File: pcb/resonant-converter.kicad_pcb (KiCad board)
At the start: 4 copper layers, 100 x 100 mm, 144 parts, among them J1 Banana_Jack_Keystone_575-8, J2 Banana_Jack_Keystone_575-8, J3 Banana_Jack_Keystone_575-8, J4 Banana_Jack_Keystone_575-8, J5 Molex_KK_1x4_0470531000, J6 JST_SH_1x4_BM04B-SRSS-TB-LF-SN, Q1 HSU30N20, Q2 HSU30N20, Q3 MDU04N010VRH, Q4 MDU04N010VRH, T1 B66206W1110T001, U1 UCC256610DDBR, U2 TEA2096T/1J, U3 78L15MG, U4 PC817X2CSP9F, U5 TL431AIDBVR, U6 INA219BIDCNR

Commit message: WIP: Layout PCB secondary side
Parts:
- moved R34 27.4 mm to (186.2, 102.2), turned to 90 degrees
- moved C49 26.9 mm to (184.8, 103.8), turned to 180 degrees
- moved R35 26.5 mm to (187.3, 102.2), turned to 90 degrees
- moved C48 25.2 mm to (186.7, 103.8), turned to 0 degrees
- moved U6 23.5 mm to (185.7, 106.2), turned to -90 degrees
- moved TP11 22.5 mm to (186.3, 119.8)
- moved TP7 22.5 mm to (190.3, 114.5)
- moved R36 21.8 mm to (184.8, 109.3), turned to 180 degrees
- moved R37 19.6 mm to (186.7, 109.3), turned to 0 degrees
- moved TP22 18.9 mm to (184.2, 116.3), turned to -90 degrees
- moved J6 18.6 mm to (185.7, 112.1), turned to 0 degrees
- moved D10 17.6 mm to (181.1, 111.3), turned to -90 degrees
- moved D9 17.5 mm to (195.3, 102.5), turned to 180 degrees
- moved kibuzzard-69E92ECD 17.4 mm to (179.9, 111.3), turned to 90 degrees
- moved R38 17.4 mm to (181.1, 113.6), turned to -90 degrees
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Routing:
- net Net-(Q4-G): track 0.00 -> 7.36 mm
- net Net-(Q3-G): track 0.00 -> 7.27 mm
- net Net-(D6-C): track 0.00 -> 7.01 mm, vias 0 -> 2
- net Net-(D5-C): track 0.00 -> 6.75 mm, vias 0 -> 2
- net /+12V_R: track 0.00 -> 3.67 mm, vias 0 -> 1
- net +12V: track 3.19 -> 5.76 mm
- net GND_ISO: track 8.42 -> 8.11 mm, vias 9 -> 38
- added copper zone on F.Cu, net +12V
- added copper zone on B.Cu, net /+12V_R
- added copper zone on F.Cu, net Net-(D5-C)
- added copper zone on F.Cu, net Net-(D6-C)

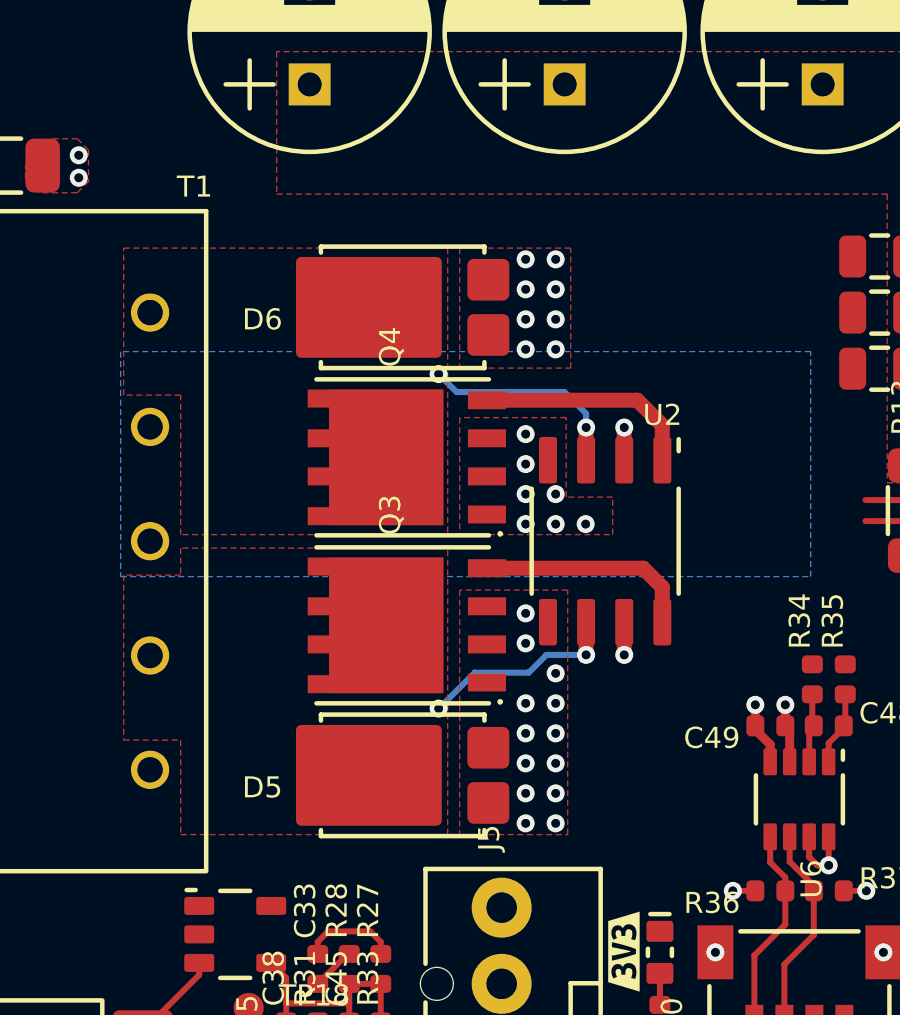
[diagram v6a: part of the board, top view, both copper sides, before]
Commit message: PCB: Layout the rectifier
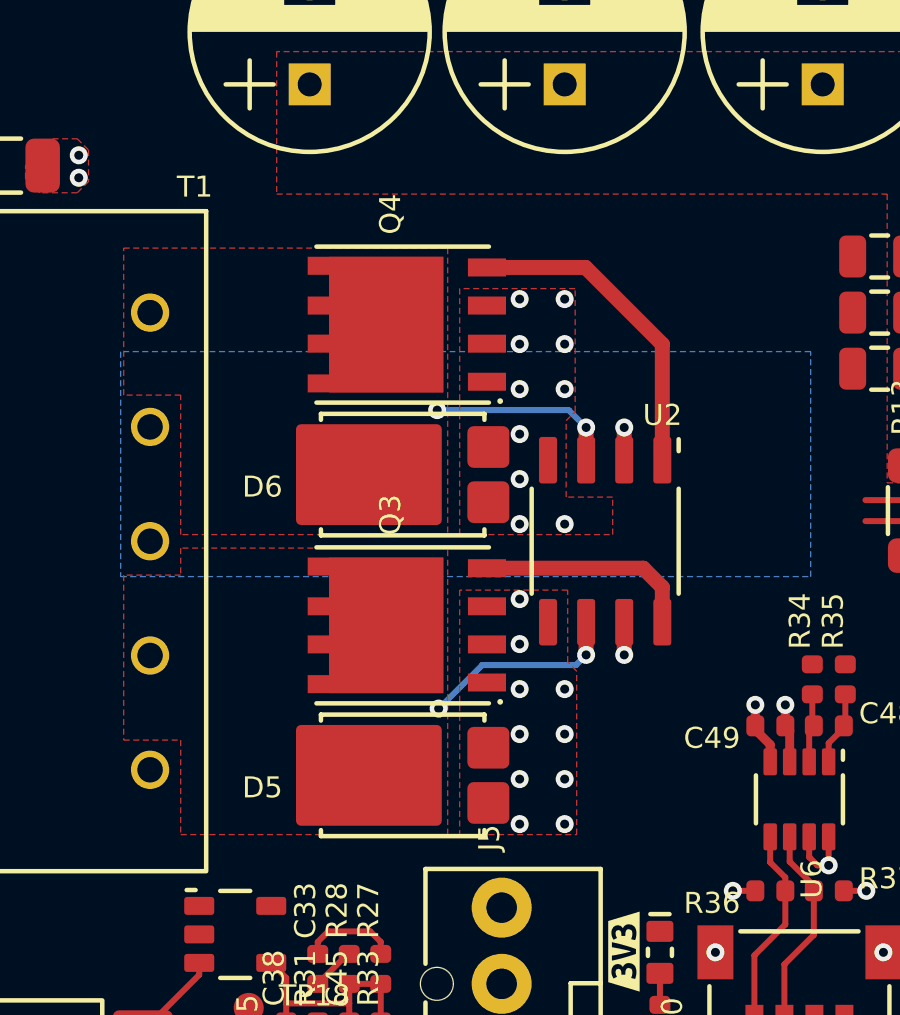
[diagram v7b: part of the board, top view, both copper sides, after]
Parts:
- moved D6 5.57 mm to (172.5, 95.4)
- moved Q4 4.43 mm to (172.5, 90.4)
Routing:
- net Net-(Q4-G): track 7.36 -> 10.8 mm
- net Net-(D6-C): track 7.01 -> 6.30 mm
- net GND_ISO: vias 38 -> 30
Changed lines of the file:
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@@
 	(footprint "DW-footprints:PowerDI-5"
 		(layer "F.Cu")
-		(at 172.5 89.825003 180)
+		(at 172.5 95.4 180)
 		(property "Reference" "D6"
 			(at 4 0 0)
@@
 	(footprint "DW-footprints:PDFN-56-8"
 		(layer "F.Cu")
-		(at 172.5 94.825003 90)
+		(at 172.5 90.4 90)
 		(descr "5x6mm Power DFN, 1.27mm pitch")
 		(tags "PDFN56, 	PDFN-56-8")
@@
 	)
 	(via
-		(at 178.6 97.05)
-		(size 0.6)
-		(drill 0.3)
-		(layers "F.Cu" "B.Cu")
-		(net 17)
-	)
-	(via
 		(at 179.885 93.83)
 		(size 0.6)
@@
 	)
 	(via
-		(at 188.525 111.325001)
-		(size 0.6)
-		(drill 0.3)
-		(layers "F.Cu" "B.Cu")
-		(net 17)
-	)
-	(via
-		(at 177.6 91.224998)
+		(at 176.4 101.05)
 		(size 0.6)
 		(drill 0.3)
@@
 	)
 	(via
-		(at 177.6 97.05)
+		(at 177.9 97.05)
 		(size 0.6)
 		(drill 0.3)
@@
 	)
 	(via
-		(at 177.6 105.025)
+		(at 188.525 111.325001)
 		(size 0.6)
 		(drill 0.3)
@@
 	)
 	(via
-		(at 177.6 102.025005)
+		(at 176.4 94.05)
 		(size 0.6)
 		(drill 0.3)
@@
 	)
 	(via
-		(at 177.6 88.225003)
+		(at 176.4 91.05)
 		(size 0.6)
 		(drill 0.3)
@@
 	)
 	(via
-		(at 176.6 105.025)
+		(at 176.4 105.55)
 		(size 0.6)
 		(drill 0.3)
@@
 	)
 	(via
-		(at 176.6 94.050005)
+		(at 177.9 91.05)
 		(size 0.6)
 		(drill 0.3)
@@
 	)
 	(via
-		(at 176.6 103.025003)
+		(at 176.4 89.55)
 		(size 0.6)
 		(drill 0.3)
@@
 	)
 	(via
-		(at 176.6 97.05)
+		(at 177.9 102.55)
 		(size 0.6)
 		(drill 0.3)
@@
 	)
 	(via
-		(at 172.46837 116.876903)
+		(at 176.4 102.55)
 		(size 0.6)
 		(drill 0.3)
@@
 	)
 	(via
-		(at 176.6 90.224998)
+		(at 176.4 99.55)
 		(size 0.6)
 		(drill 0.3)
@@
 	)
 	(via
-		(at 182.925 111.325001)
+		(at 177.9 105.55)
 		(size 0.6)
 		(drill 0.3)
@@
 	)
 	(via
-		(at 176.6 107.024998)
+		(at 176.4 97.05)
 		(size 0.6)
 		(drill 0.3)
@@
 	)
 	(via
-		(at 176.6 91.224998)
+		(at 172.46837 116.876903)
 		(size 0.6)
 		(drill 0.3)
@@
 	)
 	(via
-		(at 177.6 90.224998)
+		(at 177.9 89.55)
 		(size 0.6)
 		(drill 0.3)
@@
 	)
 	(via
-		(at 177.6 104.025003)
+		(at 182.925 111.325001)
 		(size 0.6)
 		(drill 0.3)
@@
 	)
 	(via
-		(at 176.6 89.225)
-		(size 0.6)
-		(drill 0.3)
-		(layers "F.Cu" "B.Cu")
-		(net 17)
-	)
-	(via
-		(at 176.6 96.05)
-		(size 0.6)
-		(drill 0.3)
-		(layers "F.Cu" "B.Cu")
-		(net 17)
-	)
-	(via
 		(at 187.225 114.975)
 		(size 0.6)
@@
 	)
 	(via
-		(at 176.6 101.025005)
-		(size 0.6)
-		(drill 0.3)
-		(layers "F.Cu" "B.Cu")
-		(net 17)
-	)
-	(via
 		(at 186.7 108.425)
 		(size 0.6)
@@
 	)
 	(via
-		(at 176.6 106.024998)
-		(size 0.6)
-		(drill 0.3)
-		(layers "F.Cu" "B.Cu")
-		(net 17)
-	)
-	(via
-		(at 177.6 96.05)
-		(size 0.6)
-		(drill 0.3)
-		(layers "F.Cu" "B.Cu")
-		(net 17)
-	)
-	(via
 		(at 161.703436 85.505766)
 		(size 0.6)
@@
 	)
 	(via
-		(at 176.6 100.025007)
-		(size 0.6)
-		(drill 0.3)
-		(layers "F.Cu" "B.Cu")
-		(net 17)
-	)
-	(via
-		(at 176.6 95.050002)
+		(at 177.9 92.55)
 		(size 0.6)
 		(drill 0.3)
@@
 	)
 	(via
-		(at 177.6 103.025003)
+		(at 176.4 107.05)
 		(size 0.6)
 		(drill 0.3)
@@
 	)
 	(via
-		(at 177.6 89.225)
+		(at 176.4 104.05)
 		(size 0.6)
 		(drill 0.3)
@@
 	)
 	(via
-		(at 176.6 88.225003)
+		(at 176.4 95.55)
 		(size 0.6)
 		(drill 0.3)
@@
 	)
 	(via
-		(at 177.6 107.024998)
+		(at 177.9 107.05)
 		(size 0.6)
 		(drill 0.3)
@@
 	)
 	(via
-		(at 176.6 104.025003)
+		(at 177.9 104.05)
 		(size 0.6)
 		(drill 0.3)
@@
 	)
 	(via
-		(at 177.6 106.024998)
+		(at 176.4 92.55)
 		(size 0.6)
 		(drill 0.3)
@@
 	)
 	(segment
-		(start 181.155 93.755)
-		(end 181.155 94.92)
+		(start 178.595001 88.495001)
+		(end 175.31 88.495001)
 		(width 0.5)
 		(layer "F.Cu")
@@
 	)
 	(segment
-		(start 175.31 92.920004)
-		(end 180.320004 92.920004)
+		(start 181.155 94.92)
+		(end 181.155 91.055)
 		(width 0.5)
 		(layer "F.Cu")
@@
 	)
 	(segment
-		(start 180.320004 92.920004)
-		(end 181.155 93.755)
+		(start 181.155 91.055)
+		(end 178.595001 88.495001)
 		(width 0.5)
 		(layer "F.Cu")
@@
 	)
 	(segment
-		(start 174.9 102)
-		(end 176.7 102)
-		(width 0.2)
-		(layer "B.Cu")
-		(net 21)
-	)
-	(segment
-		(start 176.7 102)
-		(end 177.290001 101.409999)
+		(start 175.15 101.75)
+		(end 178.274999 101.75)
 		(width 0.2)
 		(layer "B.Cu")
@@
 	(segment
 		(start 173.7 103.2)
-		(end 174.9 102)
+		(end 175.15 101.75)
 		(width 0.2)
 		(layer "B.Cu")
@@
 	)
 	(segment
-		(start 177.290001 101.409999)
+		(start 178.274999 101.75)
 		(end 178.615 101.409999)
 		(width 0.2)
@@
 	)
 	(via
-		(at 178.615 93.83)
+		(at 173.65 93.25)
 		(size 0.6)
 		(drill 0.3)
@@
 	)
 	(via
-		(at 173.7 92.05)
+		(at 178.615 93.83)
 		(size 0.6)
 		(drill 0.3)
@@
 	)
 	(segment
-		(start 178.615 93.365)
-		(end 178.615 93.83)
+		(start 173.65 93.25)
+		(end 178.035 93.25)
 		(width 0.2)
 		(layer "B.Cu")
@@
 	)
 	(segment
-		(start 173.7 92.05)
-		(end 174.3 92.65)
-		(width 0.2)
-		(layer "B.Cu")
-		(net 48)
-	)
-	(segment
-		(start 177.9 92.65)
-		(end 178.615 93.365)
-		(width 0.2)
-		(layer "B.Cu")
-		(net 48)
-	)
-	(segment
-		(start 174.3 92.65)
-		(end 177.9 92.65)
+		(start 178.035 93.25)
+		(end 178.615 93.83)
 		(width 0.2)
 		(layer "B.Cu")
@@
 	)
 	(zone
-		(net 17)
-		(net_name "GND_ISO")
-		(layer "F.Cu")
-		(hatch edge 0.5)
-		(priority 23)
-		(connect_pads yes
-			(clearance 0.3)
-		)
-		(min_thickness 0.25)
-		(filled_areas_thickness no)
-		(fill yes
-			(thermal_gap 0.5)
-			(thermal_bridge_width 0.5)
-			(smoothing fillet)
-			(radius 0.3)
-		)
-		(polygon
-			(pts
-				(xy 174.4 91.85) (xy 178.1 91.85) (xy 178.1 87.85) (xy 174.4 87.85)
-			)
-		)
-	)
-	(zone
 		(net 4)
 		(net_name "GND")
@@
 		(polygon
 			(pts
-				(xy 174.4 97.4) (xy 179.5 97.4) (xy 179.5 96.15) (xy 177.95 96.15) (xy 177.95 93.5) (xy 174.4 93.5)
+				(xy 174.4 97.4) (xy 179.5 97.4) (xy 179.5 96.15) (xy 177.95 96.15) (xy 177.95 93.6) (xy 178.25 93.3)
+				(xy 178.25 89.2) (xy 174.4 89.2)
 			)
 		)
@@
 		(polygon
 			(pts
-				(xy 174.4 107.4) (xy 178 107.4) (xy 178 99.25) (xy 174.4 99.25)
+				(xy 174.4 107.4) (xy 178.3 107.4) (xy 178.3 101.95) (xy 178 101.65) (xy 178 99.25) (xy 174.4 99.25)
 			)
 		)
@@
 		(priority 22)
 		(connect_pads yes
-			(clearance 0.3)
+			(clearance 0.2)
 		)
-		(min_thickness 0.25)
+		(min_thickness 0.2)
 		(filled_areas_thickness no)
 		(fill yes

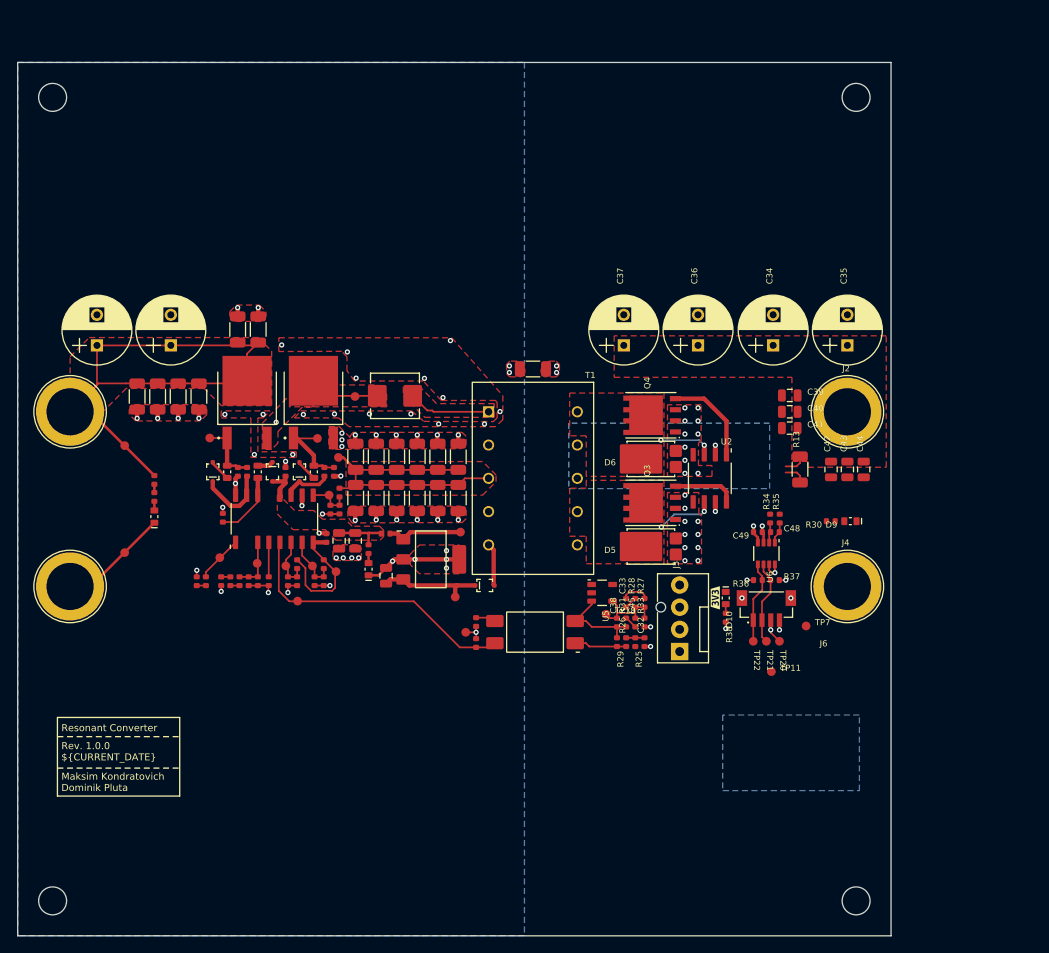
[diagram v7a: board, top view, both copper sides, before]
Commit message: PCB: Layout most of the secondary side
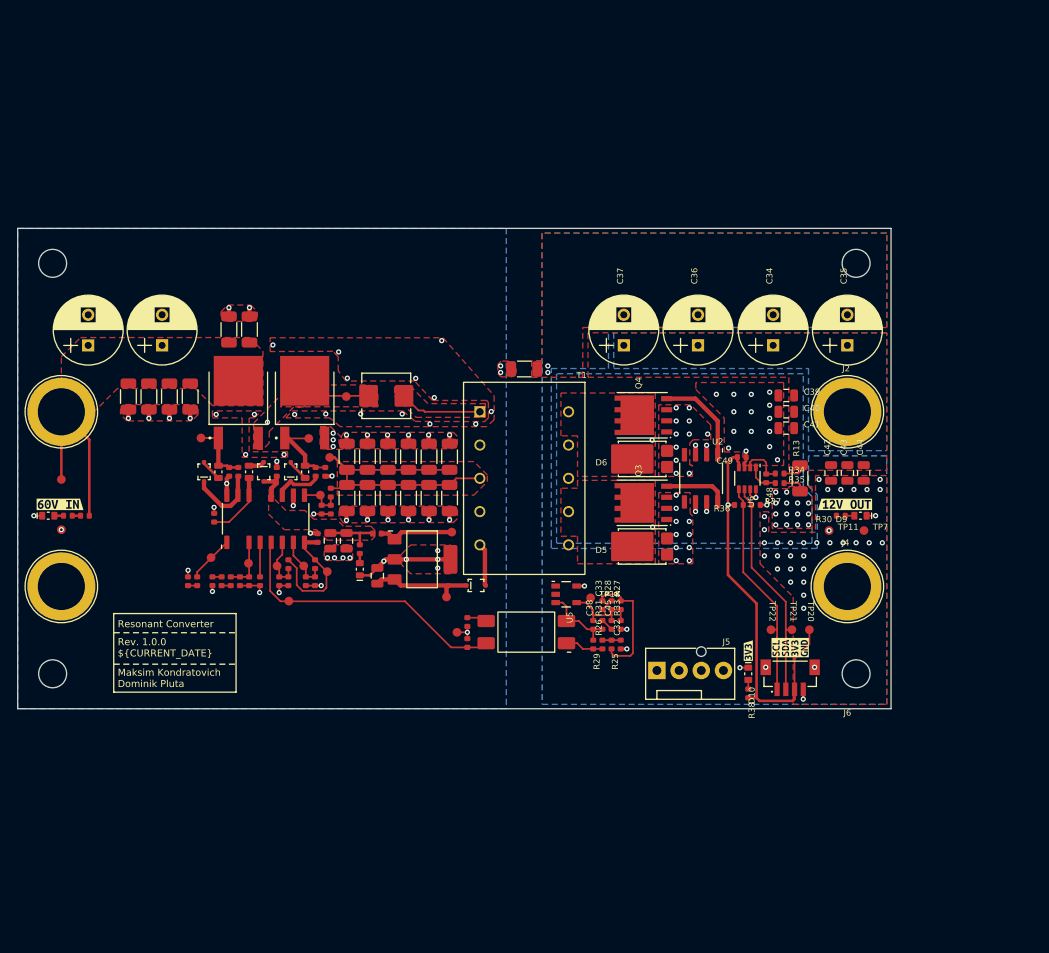
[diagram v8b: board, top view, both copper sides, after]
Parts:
- removed kibuzzard-69E92ECD: G***, kibuzzard-69E92ECD
- added kibuzzard-69F4E13D: G***, kibuzzard-69F4E13D, F.Cu at (194.7, 100.6)
- added kibuzzard-69F4E155: G***, kibuzzard-69F4E155, F.Cu at (104.8, 100.6)
- added kibuzzard-69F52FAE: G***, kibuzzard-69F52FAE, F.Cu at (183.7, 117.3)
- added kibuzzard-69F53099: G***, kibuzzard-69F53099, F.Cu at (188.4, 117.0)
- moved REF** 26.0 mm to (104.0, 120.0)
- moved REF** 26.0 mm to (196.0, 120.0)
- moved REF** 19.0 mm to (104.0, 73.0)
- moved REF** 19.0 mm to (196.0, 73.0)
- moved TP11 17.4 mm to (192.9, 103.6)
- moved TP7 12.8 mm to (196.9, 103.6)
- moved D3 12.2 mm to (103.5, 101.9), turned to 0 degrees
- moved R10 10.1 mm to (105.8, 101.9), turned to 0 degrees
- moved R38 9.05 mm to (183.7, 122.2)
- moved D10 9.05 mm to (183.7, 120.0)
- moved R6 8.94 mm to (107.7, 101.9), turned to 0 degrees
- moved R37 8.88 mm to (184.5, 100.7)
- moved R36 8.88 mm to (182.6, 100.7)
- moved U6 8.88 mm to (183.6, 97.6)
- moved C49 8.77 mm to (182.9, 95.2)
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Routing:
- net +60V: track 74.2 -> 28.4 mm
- net +3V3: track 7.19 -> 51.0 mm, vias 5 -> 2
- net /Power monitor/SCL: track 9.44 -> 25.4 mm
- net /Power monitor/SDA: track 9.75 -> 25.6 mm
- net GND: track 51.8 -> 40.1 mm, vias 52 -> 54
- net +12V: track 5.76 -> 16.4 mm
- net GND_ISO: track 8.11 -> 11.2 mm, vias 30 -> 79
- net Net-(U6-IN-): track 2.33 -> 5.06 mm
- net Net-(R26-Pad1): track 5.99 -> 4.38 mm
- net Net-(U5-K): track 10.1 -> 8.54 mm
- net Net-(U6-IN+): track 2.48 -> 3.65 mm
- net Net-(D9-A): track 0.00 -> 1.05 mm
- net /V_FB: track 8.64 -> 9.28 mm
- net /+12V_R: track 3.67 -> 3.76 mm, vias 1 -> 15
- added copper zone on B.Cu, net +12V
- added copper zone on F.Cu, net /+12V_R
- added copper zone on B.Cu, net GND_ISO
- removed copper zone on B.Cu, net +3V3
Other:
- board size 100 x 100 mm -> 100 x 55 mm
